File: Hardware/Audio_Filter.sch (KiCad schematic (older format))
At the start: 26 parts, among them U12 NE5534, U13 NE5534, U14 NE5534

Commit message: Annotated schematic
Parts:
- renumbered C52 to C50, C57 to C51, C58 to C52, C59 to C53, C62 to C54, C63 to C55, C65 to C56, C54 to C57, C64 to C58, C60 to C59, C53 to C60, C56 to C61, C55 to C62, C61 to C63, R30 to R27, R32 to R29, R34 to R30, R29 to R31, R33 to R32, R27 to R33, R31 to R34, U14 to U13, U13 to U14

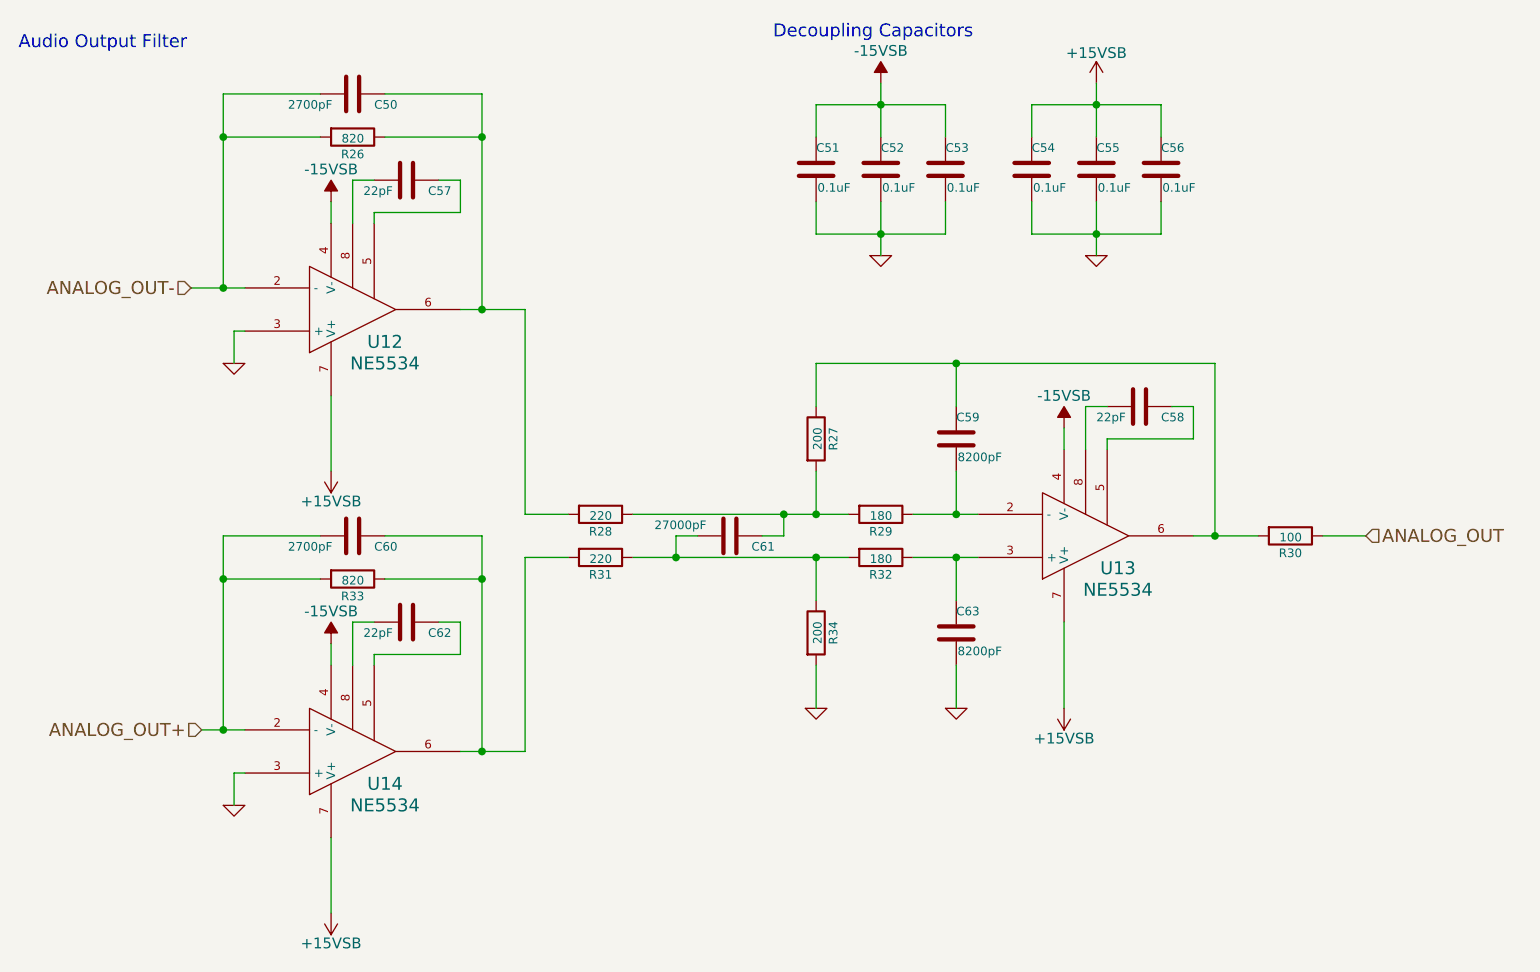
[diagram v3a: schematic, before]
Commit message: Added bluetooth pair button
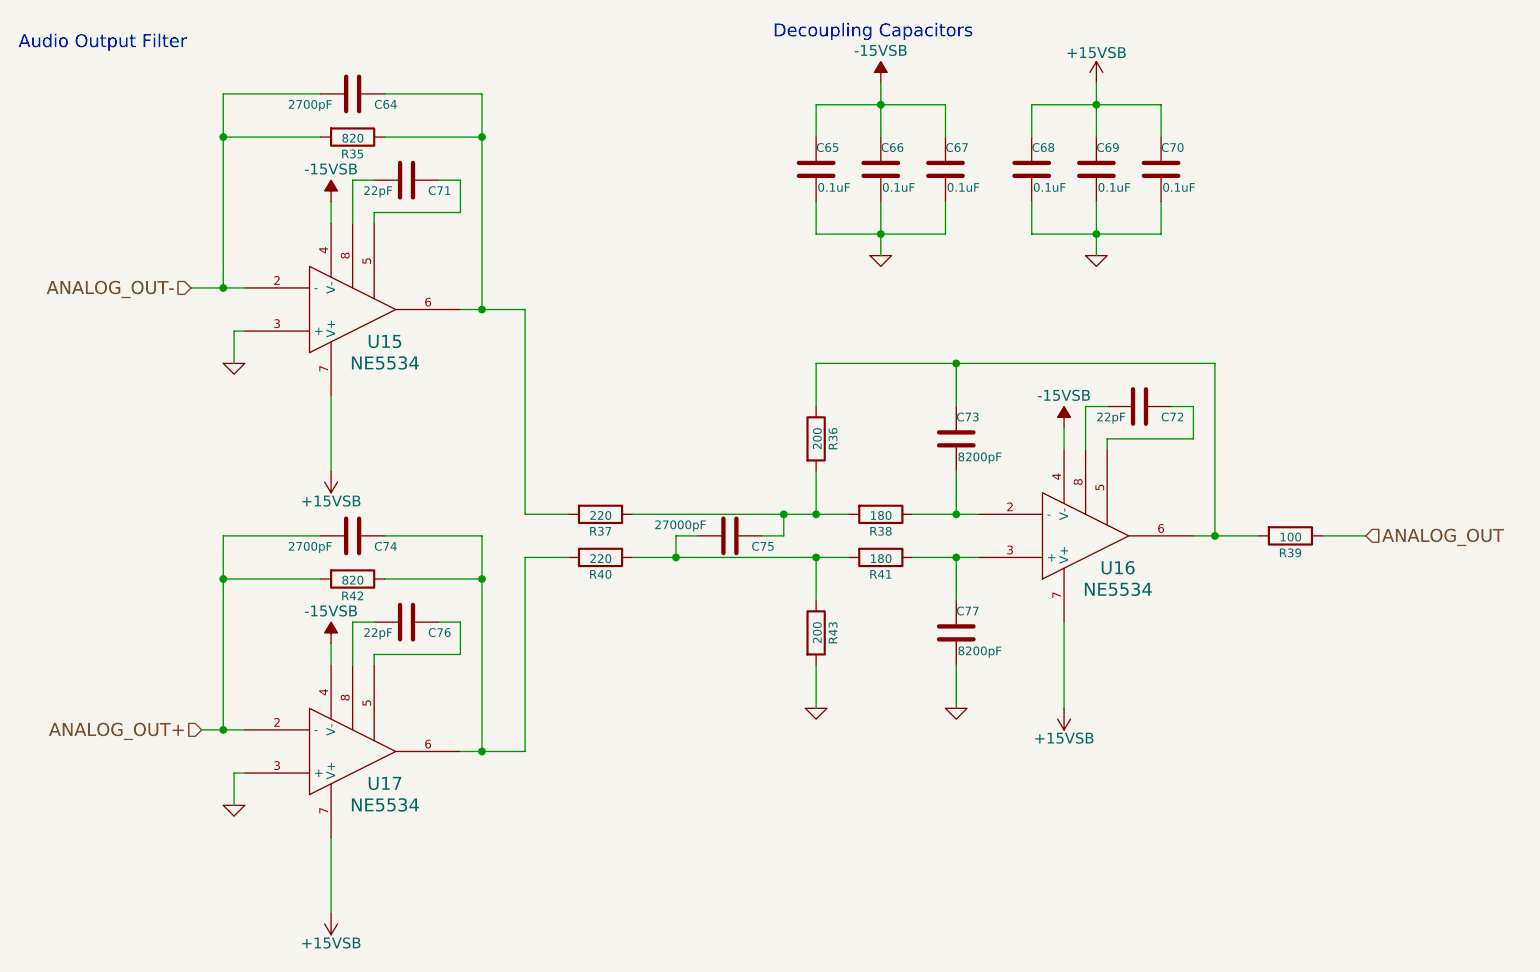
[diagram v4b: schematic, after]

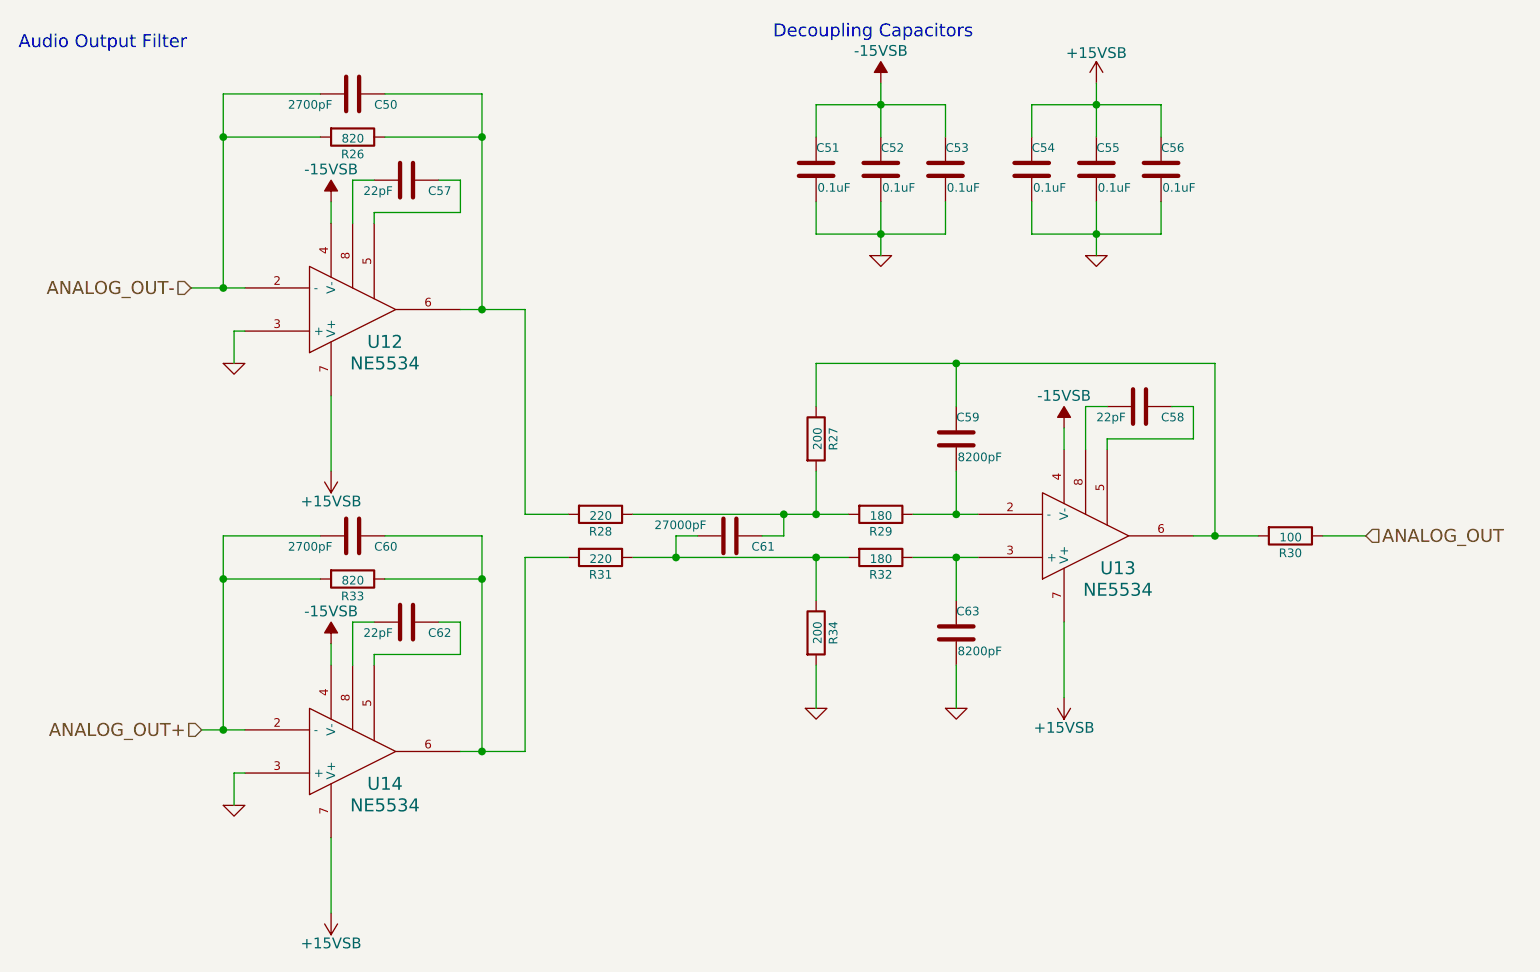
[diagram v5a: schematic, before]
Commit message: Fixed schematic errors, added muse-v2-lib
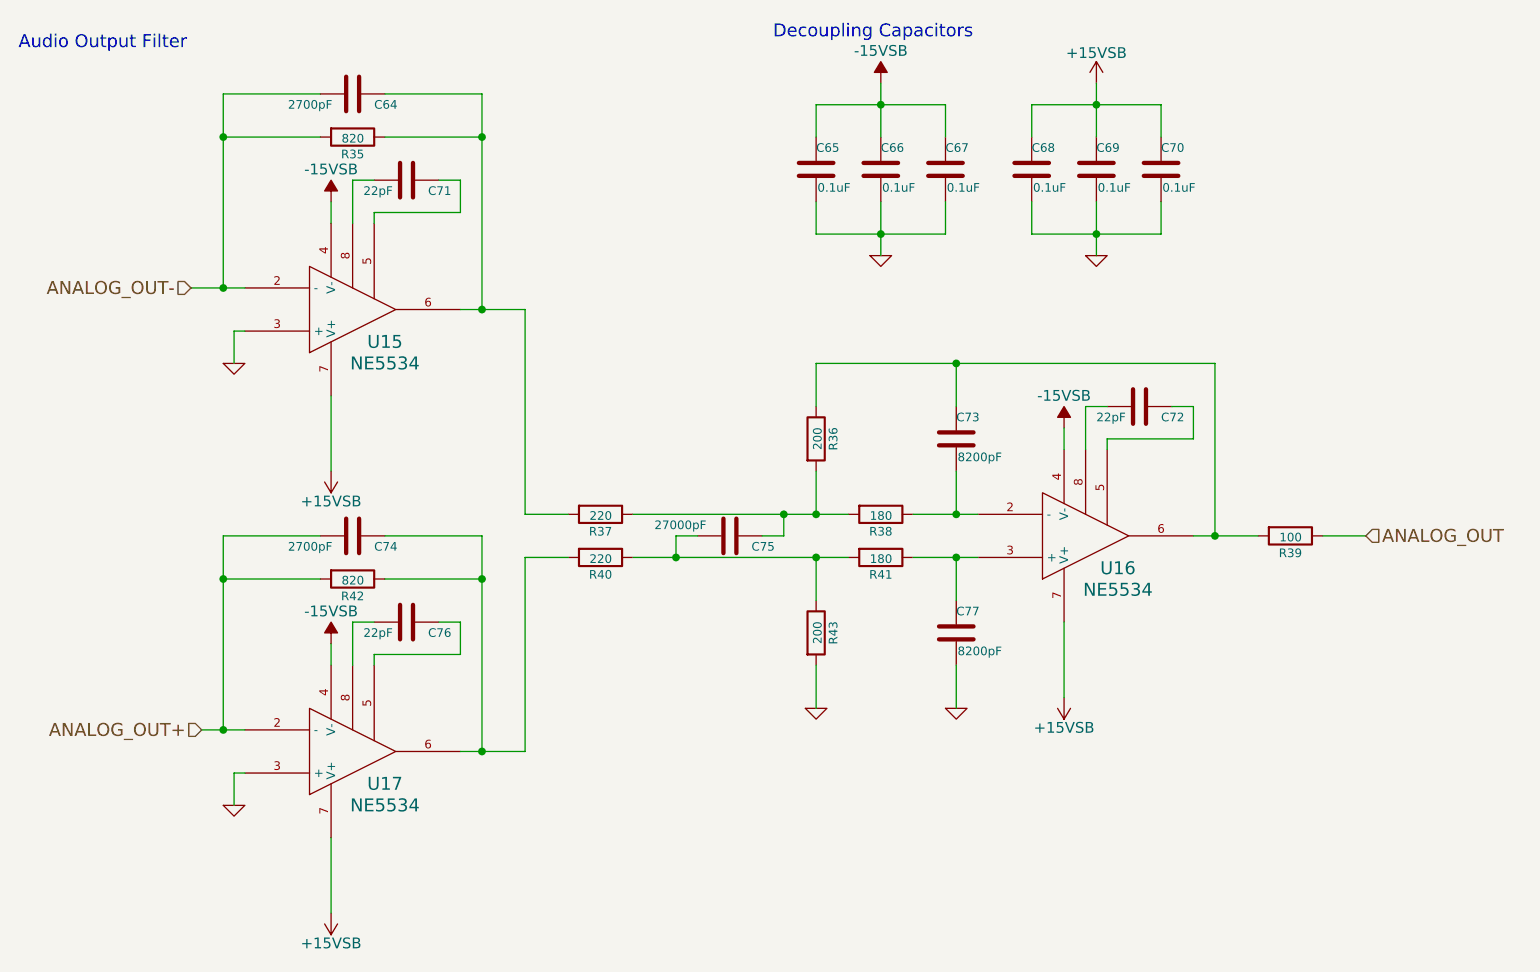
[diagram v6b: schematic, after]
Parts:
- C50, C51, C52, C53, C54, C55, C56, C57, C58, C59, C61, C62, C63: footprint (none) -> Capacitors_SMD:C_0402
- C60: footprint (none) -> Capacitors_SMD:C_0603
- R26, R27, R28, R29, R30, R31, R32, R33, R34: footprint (none) -> Resistors_SMD:R_0402

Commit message: Added proper audio connectors to schematic
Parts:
- U12, U13, U14: footprint (none) -> Housings_SOIC:SOIC-8_3.9x4.9mm_Pitch1.27mm
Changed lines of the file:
@@
 	2950 3100 3200 3100
 $Comp
-L GND-RESCUE-museV2-RESCUE-museV2 #PWR83
+L GND-RESCUE-museV2-RESCUE-museV2 #PWR078
 U 1 1 57B0E099
 P 3150 3450
-AR Path="/57F89F43/57F8A539/57B0E099" Ref="#PWR83"  Part="1"
-AR Path="/57F89F43/57F8A547/57B0E099" Ref="#PWR97"  Part="1"
-F 0 "#PWR97" H 3150 3450 30  0001 C CNN
+AR Path="/57F89F43/57F8A539/57B0E099" Ref="#PWR078"  Part="1"
+AR Path="/57F89F43/57F8A547/57B0E099" Ref="#PWR088"  Part="1"
+F 0 "#PWR088" H 3150 3450 30  0001 C CNN
 F 1 "GND" H 3150 3380 30  0001 C CNN
 F 2 "" H 3150 3450 60  0000 C CNN
@@
 	3000 5150 3200 5150
 $Comp
-L GND-RESCUE-museV2-RESCUE-museV2 #PWR90
+L GND-RESCUE-museV2-RESCUE-museV2 #PWR079
 U 1 1 57B0E0D2
 P 3150 5500
-AR Path="/57F89F43/57F8A539/57B0E0D2" Ref="#PWR90"  Part="1"
-AR Path="/57F89F43/57F8A547/57B0E0D2" Ref="#PWR104"  Part="1"
-F 0 "#PWR104" H 3150 5500 30  0001 C CNN
+AR Path="/57F89F43/57F8A539/57B0E0D2" Ref="#PWR079"  Part="1"
+AR Path="/57F89F43/57F8A547/57B0E0D2" Ref="#PWR089"  Part="1"
+F 0 "#PWR089" H 3150 5500 30  0001 C CNN
 F 1 "GND" H 3150 5430 30  0001 C CNN
 F 2 "" H 3150 5500 60  0000 C CNN
@@
 	6300 4150 6600 4150
 $Comp
-L GND-RESCUE-museV2-RESCUE-museV2 #PWR88
+L GND-RESCUE-museV2-RESCUE-museV2 #PWR080
 U 1 1 57B0E132
 P 5850 5050
-AR Path="/57F89F43/57F8A539/57B0E132" Ref="#PWR88"  Part="1"
-AR Path="/57F89F43/57F8A547/57B0E132" Ref="#PWR102"  Part="1"
-F 0 "#PWR102" H 5850 5050 30  0001 C CNN
+AR Path="/57F89F43/57F8A539/57B0E132" Ref="#PWR080"  Part="1"
+AR Path="/57F89F43/57F8A547/57B0E132" Ref="#PWR090"  Part="1"
+F 0 "#PWR090" H 5850 5050 30  0001 C CNN
 F 1 "GND" H 5850 4980 30  0001 C CNN
 F 2 "" H 5850 5050 60  0000 C CNN
@@
 Connection ~ 6500 4350
 $Comp
-L GND-RESCUE-museV2-RESCUE-museV2 #PWR89
+L GND-RESCUE-museV2-RESCUE-museV2 #PWR081
 U 1 1 57B0E15E
 P 6500 5050
-AR Path="/57F89F43/57F8A539/57B0E15E" Ref="#PWR89"  Part="1"
-AR Path="/57F89F43/57F8A547/57B0E15E" Ref="#PWR103"  Part="1"
-F 0 "#PWR103" H 6500 5050 30  0001 C CNN
+AR Path="/57F89F43/57F8A539/57B0E15E" Ref="#PWR081"  Part="1"
+AR Path="/57F89F43/57F8A547/57B0E15E" Ref="#PWR091"  Part="1"
+F 0 "#PWR091" H 6500 5050 30  0001 C CNN
 F 1 "GND" H 6500 4980 30  0001 C CNN
 F 2 "" H 6500 5050 60  0000 C CNN
@@
 F 0 "U15" H 3850 3350 60  0000 C CNN
 F 1 "NE5534" H 3850 3450 60  0000 C CNN
-F 2 "" H 3700 3200 60  0001 C CNN
+F 2 "Housings_SOIC:SOIC-8_3.9x4.9mm_Pitch1.27mm" H 3700 3200 60  0001 C CNN
 F 3 "" H 3700 3200 60  0000 C CNN
 	1    3700 3200
@@
 F 0 "U17" H 3850 5400 60  0000 C CNN
 F 1 "NE5534" H 3850 5500 60  0000 C CNN
-F 2 "" H 3700 5250 60  0001 C CNN
+F 2 "Housings_SOIC:SOIC-8_3.9x4.9mm_Pitch1.27mm" H 3700 5250 60  0001 C CNN
 F 3 "" H 3700 5250 60  0000 C CNN
 	1    3700 5250
@@
 F 0 "U16" H 7250 4400 60  0000 C CNN
 F 1 "NE5534" H 7250 4500 60  0000 C CNN
-F 2 "" H 7100 4250 60  0001 C CNN
+F 2 "Housings_SOIC:SOIC-8_3.9x4.9mm_Pitch1.27mm" H 7100 4250 60  0001 C CNN
 F 3 "" H 7100 4250 60  0000 C CNN
 	1    7100 4250
@@
 $EndComp
 $Comp
-L +15VSB #PWR85
+L +15VSB #PWR082
 U 1 1 57DC1772
 P 3600 3950
-AR Path="/57F89F43/57F8A539/57DC1772" Ref="#PWR85"  Part="1"
-AR Path="/57F89F43/57F8A547/57DC1772" Ref="#PWR99"  Part="1"
-F 0 "#PWR99" H 3600 3800 50  0001 C CNN
+AR Path="/57F89F43/57F8A539/57DC1772" Ref="#PWR082"  Part="1"
+AR Path="/57F89F43/57F8A547/57DC1772" Ref="#PWR092"  Part="1"
+F 0 "#PWR092" H 3600 3800 50  0001 C CNN
 F 1 "+15VSB" H 3600 4090 50  0000 C CNN
 F 2 "" H 3600 3950 50  0000 C CNN
@@
 $EndComp
 $Comp
-L +15VSB #PWR91
+L +15VSB #PWR083
 U 1 1 57DC1855
 P 3600 6000
-AR Path="/57F89F43/57F8A539/57DC1855" Ref="#PWR91"  Part="1"
-AR Path="/57F89F43/57F8A547/57DC1855" Ref="#PWR105"  Part="1"
-F 0 "#PWR105" H 3600 5850 50  0001 C CNN
+AR Path="/57F89F43/57F8A539/57DC1855" Ref="#PWR083"  Part="1"
+AR Path="/57F89F43/57F8A547/57DC1855" Ref="#PWR093"  Part="1"
+F 0 "#PWR093" H 3600 5850 50  0001 C CNN
 F 1 "+15VSB" H 3600 6140 50  0000 C CNN
 F 2 "" H 3600 6000 50  0000 C CNN
@@
 $EndComp
 $Comp
-L GND-RESCUE-museV2-RESCUE-museV2 #PWR81
+L GND-RESCUE-museV2-RESCUE-museV2 #PWR084
 U 1 1 57F9FACB
 P 6150 2950
-AR Path="/57F89F43/57F8A539/57F9FACB" Ref="#PWR81"  Part="1"
-AR Path="/57F89F43/57F8A547/57F9FACB" Ref="#PWR95"  Part="1"
-F 0 "#PWR95" H 6150 2950 30  0001 C CNN
+AR Path="/57F89F43/57F8A539/57F9FACB" Ref="#PWR084"  Part="1"
+AR Path="/57F89F43/57F8A547/57F9FACB" Ref="#PWR094"  Part="1"
+F 0 "#PWR094" H 6150 2950 30  0001 C CNN
 F 1 "GND" H 6150 2880 30  0001 C CNN
 F 2 "" H 6150 2950 60  0000 C CNN
@@
 $EndComp
 $Comp
-L GND-RESCUE-museV2-RESCUE-museV2 #PWR82
+L GND-RESCUE-museV2-RESCUE-museV2 #PWR085
 U 1 1 57FA15B5
 P 7150 2950
-AR Path="/57F89F43/57F8A539/57FA15B5" Ref="#PWR82"  Part="1"
-AR Path="/57F89F43/57F8A547/57FA15B5" Ref="#PWR96"  Part="1"
-F 0 "#PWR96" H 7150 2950 30  0001 C CNN
+AR Path="/57F89F43/57F8A539/57FA15B5" Ref="#PWR085"  Part="1"
+AR Path="/57F89F43/57F8A547/57FA15B5" Ref="#PWR095"  Part="1"
+F 0 "#PWR095" H 7150 2950 30  0001 C CNN
 F 1 "GND" H 7150 2880 30  0001 C CNN
 F 2 "" H 7150 2950 60  0000 C CNN
@@
 $EndComp
 $Comp
-L +15VSB #PWR79
+L +15VSB #PWR086
 U 1 1 57FFFC30
 P 7150 2150
-AR Path="/57F89F43/57F8A539/57FFFC30" Ref="#PWR79"  Part="1"
-AR Path="/57F89F43/57F8A547/57FFFC30" Ref="#PWR93"  Part="1"
-F 0 "#PWR93" H 7150 2000 50  0001 C CNN
+AR Path="/57F89F43/57F8A539/57FFFC30" Ref="#PWR086"  Part="1"
+AR Path="/57F89F43/57F8A547/57FFFC30" Ref="#PWR096"  Part="1"
+F 0 "#PWR096" H 7150 2000 50  0001 C CNN
 F 1 "+15VSB" H 7150 2290 50  0000 C CNN
 F 2 "" H 7150 2150 50  0000 C CNN
@@
 	7000 5000 7000 4650
 $Comp
-L +15VSB #PWR87
+L +15VSB #PWR087
 U 1 1 585916B9
 P 7000 5000
-AR Path="/57F89F43/57F8A539/585916B9" Ref="#PWR87"  Part="1"
-AR Path="/57F89F43/57F8A547/585916B9" Ref="#PWR101"  Part="1"
-F 0 "#PWR101" H 7000 4850 50  0001 C CNN
+AR Path="/57F89F43/57F8A539/585916B9" Ref="#PWR087"  Part="1"
+AR Path="/57F89F43/57F8A547/585916B9" Ref="#PWR097"  Part="1"
+F 0 "#PWR097" H 7000 4850 50  0001 C CNN
 F 1 "+15VSB" H 7000 5140 50  0000 C CNN
 F 2 "" H 7000 5000 50  0000 C CNN
